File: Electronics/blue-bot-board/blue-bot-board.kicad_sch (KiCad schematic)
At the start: 16 parts, among them J1 5V PS, J12 I2C0, J13 Extra GPIO, J2 X, J3 Y, J4 Z, J5 X Limit Switch, J6 Y Limit Switch, J7 Z Limit Switch, J8 Servo, SW1 RESET PB

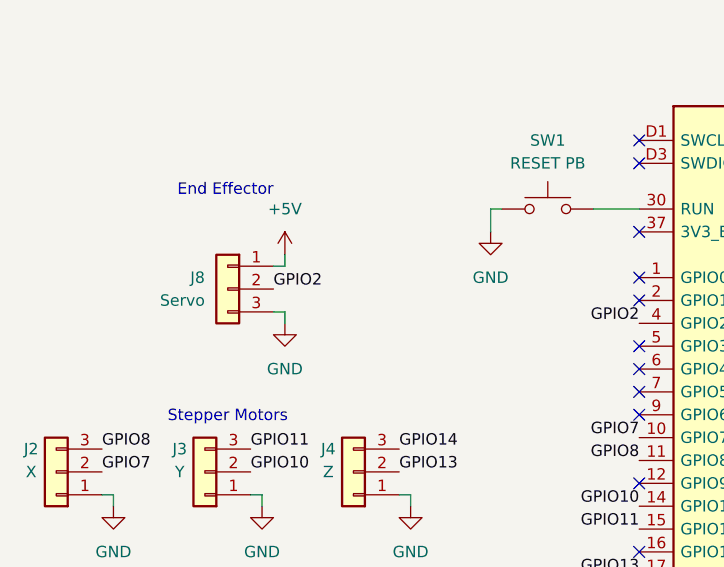
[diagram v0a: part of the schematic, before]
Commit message: Update PCB to production
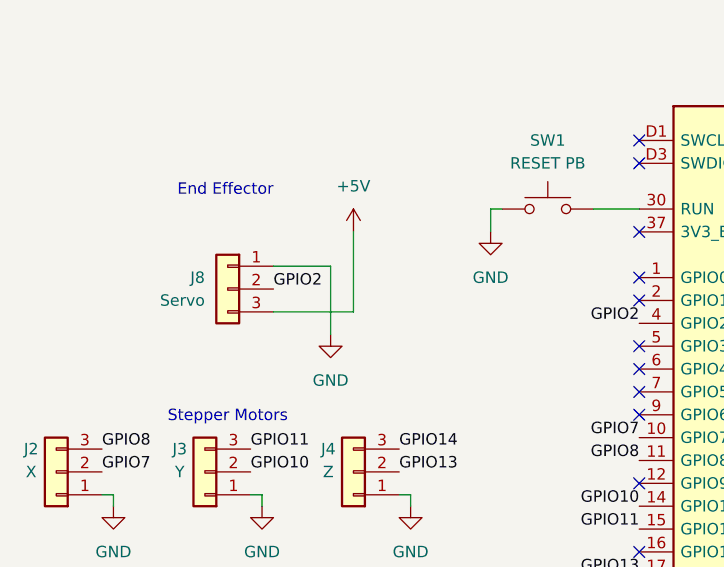
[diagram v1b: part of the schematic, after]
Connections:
- net +5V: now also J8.3 (Pin_3); no longer J8.1 (Pin_1)
- net GND: now also J8.1 (Pin_1); no longer J8.3 (Pin_3)
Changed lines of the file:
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@@
+	(wire
+		(pts
+			(xy 95.25 78.74) (xy 95.25 87.63)
+		)
+		(stroke
+			(width 0)
+			(type default)
+		)
+	)
 	(wire
 		(pts
@@
 	(wire
 		(pts
-			(xy 87.63 81.28) (xy 87.63 82.55)
-		)
-		(stroke
-			(width 0)
-			(type default)
-		)
-	)
-	(wire
-		(pts
 			(xy 196.85 80.01) (xy 196.85 82.55)
 		)
@@
 	(wire
 		(pts
-			(xy 87.63 82.55) (xy 86.36 82.55)
-		)
-		(stroke
-			(width 0)
-			(type default)
-		)
-	)
-	(wire
-		(pts
 			(xy 149.86 134.62) (xy 149.86 137.16)
 		)
@@
 	(wire
 		(pts
-			(xy 87.63 87.63) (xy 87.63 88.9)
-		)
-		(stroke
-			(width 0)
-			(type default)
-		)
-	)
-	(wire
-		(pts
 			(xy 200.66 96.52) (xy 200.66 91.44)
 		)
@@
 	(wire
 		(pts
+			(xy 95.25 87.63) (xy 86.36 87.63)
+		)
+		(stroke
+			(width 0)
+			(type default)
+		)
+	)
+	(wire
+		(pts
 			(xy 142.24 41.91) (xy 142.24 43.18)
 		)
@@
 	(wire
 		(pts
+			(xy 92.71 90.17) (xy 92.71 82.55)
+		)
+		(stroke
+			(width 0)
+			(type default)
+		)
+	)
+	(wire
+		(pts
 			(xy 196.85 93.98) (xy 196.85 99.06)
 		)
@@
 	(wire
 		(pts
-			(xy 86.36 87.63) (xy 87.63 87.63)
-		)
-		(stroke
-			(width 0)
-			(type default)
-		)
-	)
-	(wire
-		(pts
 			(xy 203.2 82.55) (xy 203.2 80.01)
 		)
@@
 		(pts
 			(xy 196.85 80.01) (xy 203.2 80.01)
+		)
+		(stroke
+			(width 0)
+			(type default)
+		)
+	)
+	(wire
+		(pts
+			(xy 92.71 82.55) (xy 86.36 82.55)
 		)
 		(stroke
@@
 	(symbol
 		(lib_id "power:+5V")
-		(at 87.63 81.28 0)
+		(at 95.25 78.74 0)
 		(unit 1)
 		(exclude_from_sim no)
@@
 		(fields_autoplaced yes)
 		(property "Reference" "#PWR08"
-			(at 87.63 85.09 0)
+			(at 95.25 82.55 0)
 			(effects
 				(font
@@
 		)
 		(property "Value" "+5V"
-			(at 87.63 76.2 0)
+			(at 95.25 73.66 0)
 			(effects
 				(font
@@
 		)
 		(property "Footprint" ""
-			(at 87.63 81.28 0)
+			(at 95.25 78.74 0)
 			(effects
 				(font
@@
 		)
 		(property "Datasheet" ""
-			(at 87.63 81.28 0)
+			(at 95.25 78.74 0)
 			(effects
 				(font
@@
 		)
 		(property "Description" "Power symbol creates a global label with name \"+5V\""
-			(at 87.63 81.28 0)
+			(at 95.25 78.74 0)
 			(effects
 				(font
@@
 	(symbol
 		(lib_id "power:GND")
-		(at 87.63 88.9 0)
+		(at 92.71 90.17 0)
 		(unit 1)
 		(exclude_from_sim no)
@@
 		(fields_autoplaced yes)
 		(property "Reference" "#PWR07"
-			(at 87.63 95.25 0)
+			(at 92.71 96.52 0)
 			(effects
 				(font
@@
 		)
 		(property "Value" "GND"
-			(at 87.63 93.98 0)
+			(at 92.71 95.25 0)
 			(effects
 				(font
@@
 		)
 		(property "Footprint" ""
-			(at 87.63 88.9 0)
+			(at 92.71 90.17 0)
 			(effects
 				(font
@@
 		)
 		(property "Datasheet" ""
-			(at 87.63 88.9 0)
+			(at 92.71 90.17 0)
 			(effects
 				(font
@@
 		)
 		(property "Description" "Power symbol creates a global label with name \"GND\" , ground"
-			(at 87.63 88.9 0)
-			(effects
-				(font
+			(at 92.71 90.17 0)
+			(effects
+				(font

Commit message: PCB Test Successful
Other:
- note added: "DIR STP"
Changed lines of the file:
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@@
+		)
+	)
+	(text "DIR\nSTP"
+		(exclude_from_sim no)
+		(at 54.61 103.632 0)
+		(effects
+			(font
+				(face "Roboto")
+				(size 1.27 1.27)
+			)
 		)
 	)
